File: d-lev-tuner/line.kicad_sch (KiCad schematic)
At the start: 4 parts

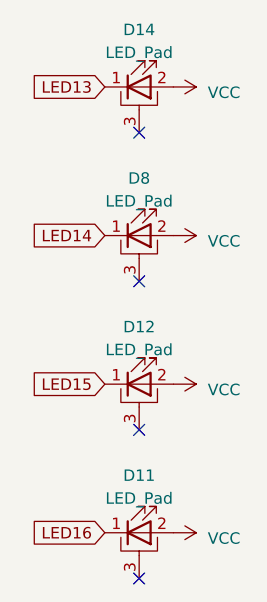
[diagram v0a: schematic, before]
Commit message: tuner: fix led footprints, reroute, place vias artistically
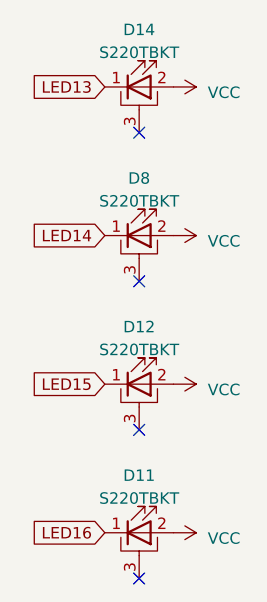
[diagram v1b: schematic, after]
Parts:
- D11, D12, D14, D8: value LED_Pad -> S220TBKT
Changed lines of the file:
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@@
       (effects (font (size 1.27 1.27)))
     )
-    (property "Value" "LED_Pad" (at 135.89 110.49 0)
+    (property "Value" "S220TBKT" (at 135.89 110.49 0)
       (effects (font (size 1.27 1.27)))
     )
@@
       (effects (font (size 1.27 1.27)) hide)
     )
-    (property "Datasheet" "~" (at 135.89 114.3 0)
+    (property "Datasheet" "https://www.mouser.com/datasheet/2/239/Lite-On-LTST-S220TBKT-1175488.pdf" (at 135.89 114.3 0)
       (effects (font (size 1.27 1.27)) hide)
     )
@@
       (effects (font (size 1.27 1.27)))
     )
-    (property "Value" "LED_Pad" (at 135.89 77.47 0)
+    (property "Value" "S220TBKT" (at 135.89 77.47 0)
       (effects (font (size 1.27 1.27)))
     )
@@
       (effects (font (size 1.27 1.27)) hide)
     )
-    (property "Datasheet" "~" (at 135.89 81.28 0)
+    (property "Datasheet" "https://www.mouser.com/datasheet/2/239/Lite-On-LTST-S220TBKT-1175488.pdf" (at 135.89 81.28 0)
       (effects (font (size 1.27 1.27)) hide)
     )
@@
       (effects (font (size 1.27 1.27)))
     )
-    (property "Value" "LED_Pad" (at 135.89 127 0)
+    (property "Value" "S220TBKT" (at 135.89 127 0)
       (effects (font (size 1.27 1.27)))
     )
@@
       (effects (font (size 1.27 1.27)) hide)
     )
-    (property "Datasheet" "~" (at 135.89 130.81 0)
+    (property "Datasheet" "https://www.mouser.com/datasheet/2/239/Lite-On-LTST-S220TBKT-1175488.pdf" (at 135.89 130.81 0)
       (effects (font (size 1.27 1.27)) hide)
     )
@@
       (effects (font (size 1.27 1.27)))
     )
-    (property "Value" "LED_Pad" (at 135.89 93.98 0)
+    (property "Value" "S220TBKT" (at 135.89 93.98 0)
       (effects (font (size 1.27 1.27)))
     )
@@
       (effects (font (size 1.27 1.27)) hide)
     )
-    (property "Datasheet" "~" (at 135.89 97.79 0)
+    (property "Datasheet" "https://www.mouser.com/datasheet/2/239/Lite-On-LTST-S220TBKT-1175488.pdf" (at 135.89 97.79 0)
       (effects (font (size 1.27 1.27)) hide)
     )

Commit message: tuner: fixed led footprints
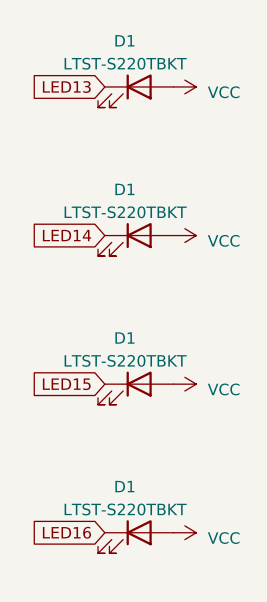
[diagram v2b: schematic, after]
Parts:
- removed D11, D12, D14, D8: S220TBKT, d-lev:S220TBKT, symbol Device:LED_Pad
- added D1 (x4): LTST-S220TBKT, d-lev:S220TBKT, symbol Device:LED
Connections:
- net LED13: now also D1.1 (K)
- net LED14: now also D1.1 (K)
- net LED15: now also D1.1 (K)
- net LED16: now also D1.1 (K)
- net VCC: now also D1.2 (A), D1.2 (A), D1.2 (A), D1.2 (A)
- no-connect marks 4 -> 0
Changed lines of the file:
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@@
 (kicad_sch (version 20230121) (generator eeschema)
   (paper "A4")
-  (no_connect (at 135.89 86.36))
-  (no_connect (at 135.89 102.87))
-  (no_connect (at 135.89 119.38))
-  (no_connect (at 135.89 135.89))
   (global_label "LED15" (shape input) (at 132.08 114.3 180) (fields_autoplaced)
     (effects (font (size 1.27 1.27)) (justify right))
@@
     (property "Intersheetrefs" "${INTERSHEET_REFS}" (at 123.9623 130.81 0)
       (effects (font (size 1.27 1.27)) (justify right) hide)
+    )
+  )
+  (symbol (lib_id "Device:LED") (at 135.89 97.79 0) (unit 1)
+    (in_bom yes) (on_board yes) (dnp no) (fields_autoplaced)
+    (property "Reference" "D1" (at 134.3025 92.71 0)
+      (effects (font (size 1.27 1.27)))
+    )
+    (property "Value" "LTST-S220TBKT" (at 134.3025 95.25 0)
+      (effects (font (size 1.27 1.27)))
+    )
+    (property "Footprint" "d-lev:S220TBKT" (at 135.89 97.79 0)
+      (effects (font (size 1.27 1.27)) hide)
+    )
+    (property "Datasheet" "https://www.mouser.com/datasheet/2/239/Lite-On-LTST-S220TBKT-1175488.pdf" (at 135.89 97.79 0)
+      (effects (font (size 1.27 1.27)) hide)
+    )
+    (pin "1")
+    (pin "2")
+    (instances
+      (project "d-lev-tuner"
+        (path "/d0a63483-9262-4daa-933b-19ce0ffbb204"
+          (reference "D1") (unit 1)
+        )
+        (path "/d0a63483-9262-4daa-933b-19ce0ffbb204/1928c8f4-6cf4-4737-93cd-521227fbe60f"
+          (reference "D2") (unit 1)
+        )
+        (path "/d0a63483-9262-4daa-933b-19ce0ffbb204/2f59d682-5d95-40dc-ad14-fff6ed248fda"
+          (reference "D13") (unit 1)
+        )
+      )
     )
   )
@@
     )
   )
+  (symbol (lib_id "Device:LED") (at 135.89 130.81 0) (unit 1)
+    (in_bom yes) (on_board yes) (dnp no) (fields_autoplaced)
+    (property "Reference" "D1" (at 134.3025 125.73 0)
+      (effects (font (size 1.27 1.27)))
+    )
+    (property "Value" "LTST-S220TBKT" (at 134.3025 128.27 0)
+      (effects (font (size 1.27 1.27)))
+    )
+    (property "Footprint" "d-lev:S220TBKT" (at 135.89 130.81 0)
+      (effects (font (size 1.27 1.27)) hide)
+    )
+    (property "Datasheet" "https://www.mouser.com/datasheet/2/239/Lite-On-LTST-S220TBKT-1175488.pdf" (at 135.89 130.81 0)
+      (effects (font (size 1.27 1.27)) hide)
+    )
+    (pin "1")
+    (pin "2")
+    (instances
+      (project "d-lev-tuner"
+        (path "/d0a63483-9262-4daa-933b-19ce0ffbb204"
+          (reference "D1") (unit 1)
+        )
+        (path "/d0a63483-9262-4daa-933b-19ce0ffbb204/1928c8f4-6cf4-4737-93cd-521227fbe60f"
+          (reference "D2") (unit 1)
+        )
+        (path "/d0a63483-9262-4daa-933b-19ce0ffbb204/2f59d682-5d95-40dc-ad14-fff6ed248fda"
+          (reference "D15") (unit 1)
+        )
+      )
+    )
+  )
   (symbol (lib_id "power:VCC") (at 139.7 81.28 270) (unit 1)
     (in_bom yes) (on_board yes) (dnp no) (fields_autoplaced)
@@
     )
   )
-  (symbol (lib_id "Device:LED_Pad") (at 135.89 114.3 0) (unit 1)
-    (in_bom yes) (on_board yes) (dnp no) (fields_autoplaced)
-    (property "Reference" "D12" (at 135.89 107.95 0)
-      (effects (font (size 1.27 1.27)))
-    )
-    (property "Value" "S220TBKT" (at 135.89 110.49 0)
-      (effects (font (size 1.27 1.27)))
-    )
-    (property "Footprint" "d-lev:S220TBKT" (at 135.89 114.3 0)
-      (effects (font (size 1.27 1.27)) hide)
-    )
-    (property "Datasheet" "https://www.mouser.com/datasheet/2/239/Lite-On-LTST-S220TBKT-1175488.pdf" (at 135.89 114.3 0)
-      (effects (font (size 1.27 1.27)) hide)
-    )
-    (pin "1")
-    (pin "2")
-    (pin "3")
-    (instances
-      (project "d-lev-tuner"
-        (path "/d0a63483-9262-4daa-933b-19ce0ffbb204"
-          (reference "D12") (unit 1)
-        )
-        (path "/d0a63483-9262-4daa-933b-19ce0ffbb204/2f59d682-5d95-40dc-ad14-fff6ed248fda"
-          (reference "D15") (unit 1)
+  (symbol (lib_id "Device:LED") (at 135.89 81.28 0) (unit 1)
+    (in_bom yes) (on_board yes) (dnp no) (fields_autoplaced)
+    (property "Reference" "D1" (at 134.3025 76.2 0)
+      (effects (font (size 1.27 1.27)))
+    )
+    (property "Value" "LTST-S220TBKT" (at 134.3025 78.74 0)
+      (effects (font (size 1.27 1.27)))
+    )
+    (property "Footprint" "d-lev:S220TBKT" (at 135.89 81.28 0)
+      (effects (font (size 1.27 1.27)) hide)
+    )
+    (property "Datasheet" "https://www.mouser.com/datasheet/2/239/Lite-On-LTST-S220TBKT-1175488.pdf" (at 135.89 81.28 0)
+      (effects (font (size 1.27 1.27)) hide)
+    )
+    (pin "1")
+    (pin "2")
+    (instances
+      (project "d-lev-tuner"
+        (path "/d0a63483-9262-4daa-933b-19ce0ffbb204"
+          (reference "D1") (unit 1)
+        )
+        (path "/d0a63483-9262-4daa-933b-19ce0ffbb204/1928c8f4-6cf4-4737-93cd-521227fbe60f"
+          (reference "D2") (unit 1)
+        )
+        (path "/d0a63483-9262-4daa-933b-19ce0ffbb204/2f59d682-5d95-40dc-ad14-fff6ed248fda"
+          (reference "D17") (unit 1)
         )
       )
@@
     )
   )
-  (symbol (lib_id "Device:LED_Pad") (at 135.89 81.28 0) (unit 1)
-    (in_bom yes) (on_board yes) (dnp no) (fields_autoplaced)
-    (property "Reference" "D14" (at 135.89 74.93 0)
-      (effects (font (size 1.27 1.27)))
-    )
-    (property "Value" "S220TBKT" (at 135.89 77.47 0)
-      (effects (font (size 1.27 1.27)))
-    )
-    (property "Footprint" "d-lev:S220TBKT" (at 135.89 81.28 0)
-      (effects (font (size 1.27 1.27)) hide)
-    )
-    (property "Datasheet" "https://www.mouser.com/datasheet/2/239/Lite-On-LTST-S220TBKT-1175488.pdf" (at 135.89 81.28 0)
-      (effects (font (size 1.27 1.27)) hide)
-    )
-    (pin "1")
-    (pin "2")
-    (pin "3")
-    (instances
-      (project "d-lev-tuner"
-        (path "/d0a63483-9262-4daa-933b-19ce0ffbb204"
-          (reference "D14") (unit 1)
-        )
-        (path "/d0a63483-9262-4daa-933b-19ce0ffbb204/2f59d682-5d95-40dc-ad14-fff6ed248fda"
-          (reference "D13") (unit 1)
-        )
-      )
-    )
-  )
-  (symbol (lib_id "Device:LED_Pad") (at 135.89 130.81 0) (unit 1)
-    (in_bom yes) (on_board yes) (dnp no) (fields_autoplaced)
-    (property "Reference" "D11" (at 135.89 124.46 0)
-      (effects (font (size 1.27 1.27)))
-    )
-    (property "Value" "S220TBKT" (at 135.89 127 0)
-      (effects (font (size 1.27 1.27)))
-    )
-    (property "Footprint" "d-lev:S220TBKT" (at 135.89 130.81 0)
-      (effects (font (size 1.27 1.27)) hide)
-    )
-    (property "Datasheet" "https://www.mouser.com/datasheet/2/239/Lite-On-LTST-S220TBKT-1175488.pdf" (at 135.89 130.81 0)
-      (effects (font (size 1.27 1.27)) hide)
-    )
-    (pin "1")
-    (pin "2")
-    (pin "3")
-    (instances
-      (project "d-lev-tuner"
-        (path "/d0a63483-9262-4daa-933b-19ce0ffbb204"
-          (reference "D11") (unit 1)
-        )
-        (path "/d0a63483-9262-4daa-933b-19ce0ffbb204/2f59d682-5d95-40dc-ad14-fff6ed248fda"
-          (reference "D16") (unit 1)
-        )
-      )
-    )
-  )
-  (symbol (lib_id "Device:LED_Pad") (at 135.89 97.79 0) (unit 1)
-    (in_bom yes) (on_board yes) (dnp no) (fields_autoplaced)
-    (property "Reference" "D8" (at 135.89 91.44 0)
-      (effects (font (size 1.27 1.27)))
-    )
-    (property "Value" "S220TBKT" (at 135.89 93.98 0)
-      (effects (font (size 1.27 1.27)))
-    )
-    (property "Footprint" "d-lev:S220TBKT" (at 135.89 97.79 0)
-      (effects (font (size 1.27 1.27)) hide)
-    )
-    (property "Datasheet" "https://www.mouser.com/datasheet/2/239/Lite-On-LTST-S220TBKT-1175488.pdf" (at 135.89 97.79 0)
-      (effects (font (size 1.27 1.27)) hide)
-    )
-    (pin "1")
-    (pin "2")
-    (pin "3")
-    (instances
-      (project "d-lev-tuner"
-        (path "/d0a63483-9262-4daa-933b-19ce0ffbb204"
-          (reference "D8") (unit 1)
-        )
-        (path "/d0a63483-9262-4daa-933b-19ce0ffbb204/2f59d682-5d95-40dc-ad14-fff6ed248fda"
+  (symbol (lib_id "Device:LED") (at 135.89 114.3 0) (unit 1)
+    (in_bom yes) (on_board yes) (dnp no) (fields_autoplaced)
+    (property "Reference" "D1" (at 134.3025 109.22 0)
+      (effects (font (size 1.27 1.27)))
+    )
+    (property "Value" "LTST-S220TBKT" (at 134.3025 111.76 0)
+      (effects (font (size 1.27 1.27)))
+    )
+    (property "Footprint" "d-lev:S220TBKT" (at 135.89 114.3 0)
+      (effects (font (size 1.27 1.27)) hide)
+    )
+    (property "Datasheet" "https://www.mouser.com/datasheet/2/239/Lite-On-LTST-S220TBKT-1175488.pdf" (at 135.89 114.3 0)
+      (effects (font (size 1.27 1.27)) hide)
+    )
+    (pin "1")
+    (pin "2")
+    (instances
+      (project "d-lev-tuner"
+        (path "/d0a63483-9262-4daa-933b-19ce0ffbb204"
+          (reference "D1") (unit 1)
+        )
+        (path "/d0a63483-9262-4daa-933b-19ce0ffbb204/1928c8f4-6cf4-4737-93cd-521227fbe60f"
+          (reference "D2") (unit 1)
+        )
+        (path "/d0a63483-9262-4daa-933b-19ce0ffbb204/2f59d682-5d95-40dc-ad14-fff6ed248fda"

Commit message: Add iBOMs and additional part numbers
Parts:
- D1: MPN (none) -> LTST-S220TBKT; Supplier (none) -> Mouser; Supplier URL (none) -> https://www.mouser.com/ProductDetail/859-LTST-S220TBKT
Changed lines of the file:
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@@
+      (effects (font (size 1.27 1.27)) hide)
+    )
+    (property "MPN" "LTST-S220TBKT" (at 135.89 97.79 0)
+      (effects (font (size 1.27 1.27)) hide)
+    )
+    (property "Supplier" "Mouser" (at 135.89 97.79 0)
+      (effects (font (size 1.27 1.27)) hide)
+    )
+    (property "Supplier URL" "https://www.mouser.com/ProductDetail/859-LTST-S220TBKT" (at 135.89 97.79 0)
+      (effects (font (size 1.27 1.27)) hide)
+    )
+    (property "Notes" "" (at 135.89 97.79 0)
+      (effects (font (size 1.27 1.27)) hide)
+    )
+    (property "Supplier Alt" "" (at 135.89 97.79 0)
+      (effects (font (size 1.27 1.27)) hide)
+    )
+    (property "Supplier Alt URL" "" (at 135.89 97.79 0)
       (effects (font (size 1.27 1.27)) hide)
     )
@@
       (effects (font (size 1.27 1.27)) hide)
     )
+    (property "MPN" "LTST-S220TBKT" (at 135.89 130.81 0)
+      (effects (font (size 1.27 1.27)) hide)
+    )
+    (property "Supplier" "Mouser" (at 135.89 130.81 0)
+      (effects (font (size 1.27 1.27)) hide)
+    )
+    (property "Supplier URL" "https://www.mouser.com/ProductDetail/859-LTST-S220TBKT" (at 135.89 130.81 0)
+      (effects (font (size 1.27 1.27)) hide)
+    )
+    (property "Notes" "" (at 135.89 130.81 0)
+      (effects (font (size 1.27 1.27)) hide)
+    )
+    (property "Supplier Alt" "" (at 135.89 130.81 0)
+      (effects (font (size 1.27 1.27)) hide)
+    )
+    (property "Supplier Alt URL" "" (at 135.89 130.81 0)
+      (effects (font (size 1.27 1.27)) hide)
+    )
     (pin "1")
     (pin "2")
@@
       (effects (font (size 1.27 1.27)) hide)
     )
+    (property "MPN" "LTST-S220TBKT" (at 135.89 81.28 0)
+      (effects (font (size 1.27 1.27)) hide)
+    )
+    (property "Supplier" "Mouser" (at 135.89 81.28 0)
+      (effects (font (size 1.27 1.27)) hide)
+    )
+    (property "Supplier URL" "https://www.mouser.com/ProductDetail/859-LTST-S220TBKT" (at 135.89 81.28 0)
+      (effects (font (size 1.27 1.27)) hide)
+    )
+    (property "Notes" "" (at 135.89 81.28 0)
+      (effects (font (size 1.27 1.27)) hide)
+    )
+    (property "Supplier Alt" "" (at 135.89 81.28 0)
+      (effects (font (size 1.27 1.27)) hide)
+    )
+    (property "Supplier Alt URL" "" (at 135.89 81.28 0)
+      (effects (font (size 1.27 1.27)) hide)
+    )
     (pin "1")
     (pin "2")
@@
       (effects (font (size 1.27 1.27)) hide)
     )
+    (property "MPN" "LTST-S220TBKT" (at 135.89 114.3 0)
+      (effects (font (size 1.27 1.27)) hide)
+    )
+    (property "Supplier" "Mouser" (at 135.89 114.3 0)
+      (effects (font (size 1.27 1.27)) hide)
+    )
+    (property "Supplier URL" "https://www.mouser.com/ProductDetail/859-LTST-S220TBKT" (at 135.89 114.3 0)
+      (effects (font (size 1.27 1.27)) hide)
+    )
+    (property "Notes" "" (at 135.89 114.3 0)
+      (effects (font (size 1.27 1.27)) hide)
+    )
+    (property "Supplier Alt" "" (at 135.89 114.3 0)
+      (effects (font (size 1.27 1.27)) hide)
+    )
+    (property "Supplier Alt URL" "" (at 135.89 114.3 0)
+      (effects (font (size 1.27 1.27)) hide)
+    )
